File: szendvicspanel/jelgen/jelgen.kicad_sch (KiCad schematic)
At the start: 24 parts, among them J1 Conn_01x04_Pin, U1 TL072, U2 TL072

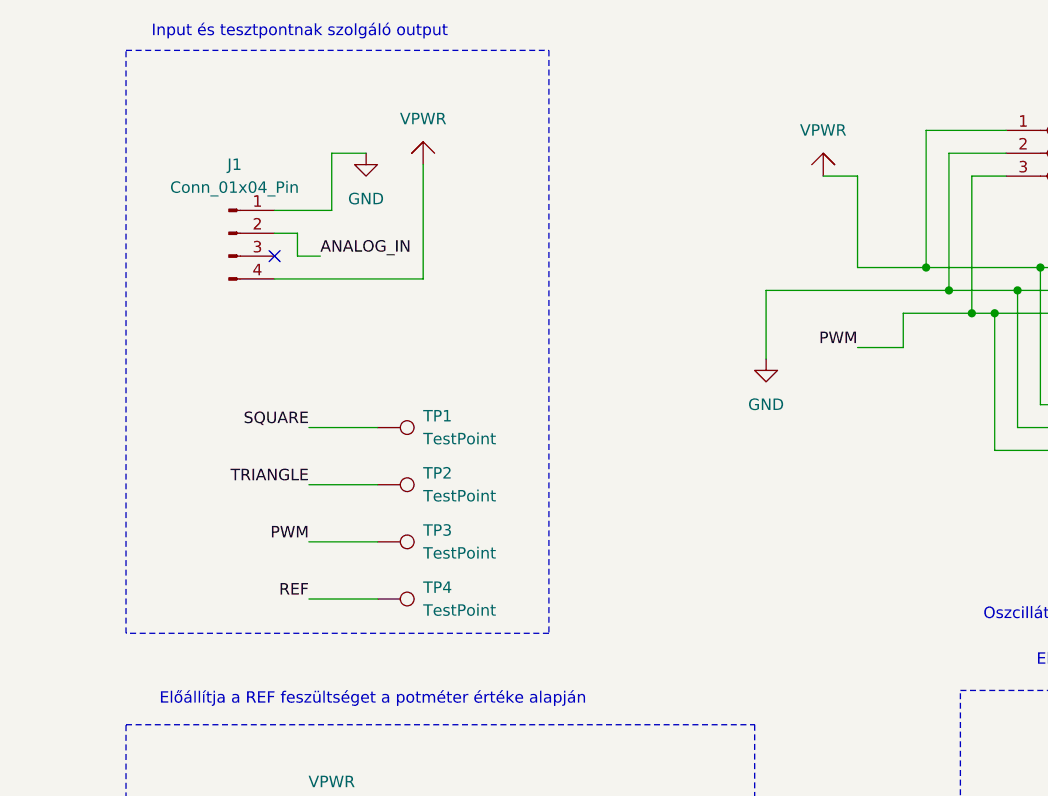
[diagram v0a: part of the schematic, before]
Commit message: Átalakítás a H-híd panel szélességére, hanging +5V input pin
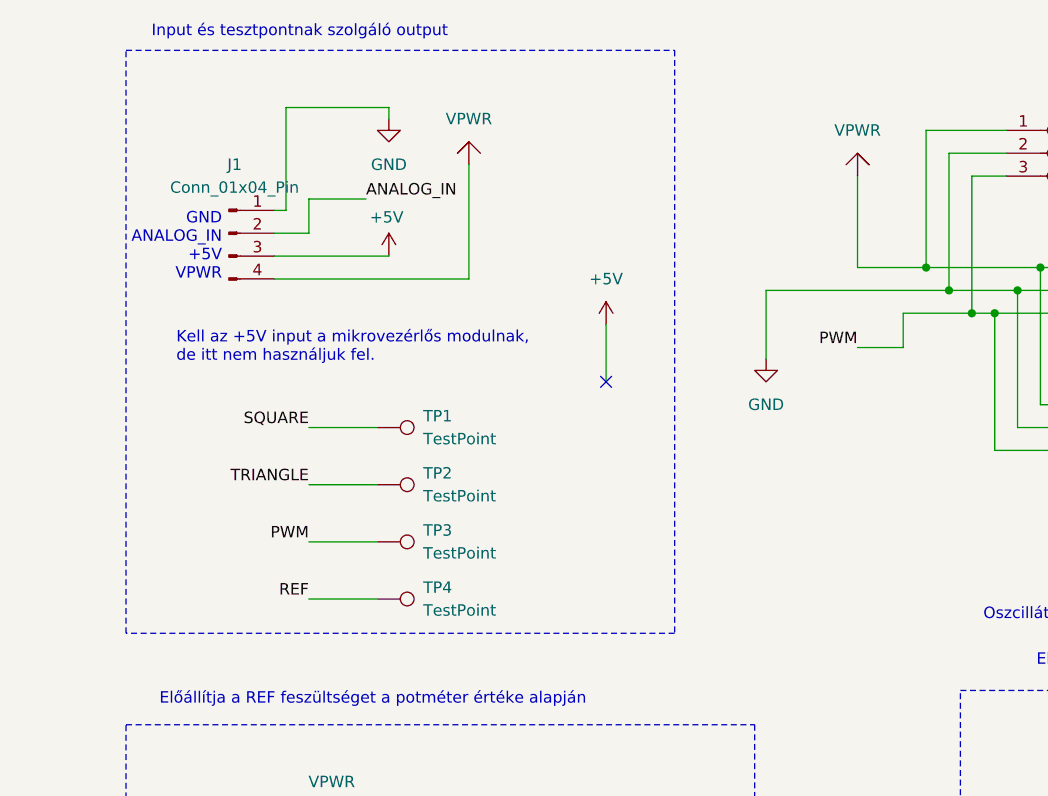
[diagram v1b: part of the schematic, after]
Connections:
- net +5V: now reaches J1.3 (Pin_3)
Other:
- note added: "GND ANALOG_IN +5V VPWR"
- note added: "Kell az +5V input a mikrovezérlős modulnak, de itt nem használjuk fel."
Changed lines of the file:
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@@
 	(rectangle
 		(start 30.48 22.86)
-		(end 77.47 87.63)
+		(end 91.44 87.63)
 		(stroke
 			(width 0.127)
@@
 		)
 	)
+	(text "GND\nANALOG_IN\n+5V\nVPWR"
+		(exclude_from_sim no)
+		(at 41.148 44.704 0)
+		(effects
+			(font
+				(size 1.27 1.27)
+			)
+			(justify right)
+		)
+	)
 	(text "Az oszcillátor háromszögjeléből és az analóg bemenetből előállítja a PWM jelet"
 		(exclude_from_sim no)
@@
 		)
 	)
+	(text "Kell az +5V input a mikrovezérlős modulnak,\nde itt nem használjuk fel."
+		(exclude_from_sim no)
+		(at 36.068 55.88 0)
+		(effects
+			(font
+				(size 1.27 1.27)
+			)
+			(justify left)
+		)
+	)
 	(text "8 db PWM output, 8 db H-hídhoz"
 		(exclude_from_sim no)
@@
 	)
 	(no_connect
-		(at 46.99 45.72)
+		(at 83.82 59.69)
 	)
 	(no_connect
@@
 	(wire
 		(pts
-			(xy 63.5 48.26) (xy 46.99 48.26)
+			(xy 68.58 48.26) (xy 46.99 48.26)
 		)
 		(stroke
@@
 	(wire
 		(pts
+			(xy 46.99 45.72) (xy 59.69 45.72)
+		)
+		(stroke
+			(width 0)
+			(type default)
+		)
+	)
+	(wire
+		(pts
 			(xy 153.67 46.99) (xy 166.37 46.99)
 		)
@@
 	(wire
 		(pts
-			(xy 53.34 34.29) (xy 57.15 34.29)
+			(xy 48.26 29.21) (xy 59.69 29.21)
+		)
+		(stroke
+			(width 0)
+			(type default)
+		)
+	)
+	(wire
+		(pts
+			(xy 59.69 29.21) (xy 59.69 30.48)
 		)
 		(stroke
@@
 	(wire
 		(pts
-			(xy 53.34 40.64) (xy 46.99 40.64)
+			(xy 48.26 40.64) (xy 46.99 40.64)
 		)
 		(stroke
@@
 	(wire
 		(pts
-			(xy 49.53 43.18) (xy 46.99 43.18)
+			(xy 50.8 39.37) (xy 57.15 39.37)
 		)
 		(stroke
@@
 	(wire
 		(pts
-			(xy 53.34 34.29) (xy 53.34 40.64)
+			(xy 48.26 29.21) (xy 48.26 40.64)
 		)
 		(stroke
@@
 	(wire
 		(pts
-			(xy 111.76 36.83) (xy 107.95 36.83)
-		)
-		(stroke
-			(width 0)
-			(type default)
-		)
-	)
-	(wire
-		(pts
 			(xy 102.87 175.26) (xy 93.98 175.26)
 		)
@@
 	(wire
 		(pts
+			(xy 50.8 43.18) (xy 46.99 43.18)
+		)
+		(stroke
+			(width 0)
+			(type default)
+		)
+	)
+	(wire
+		(pts
 			(xy 186.69 46.99) (xy 199.39 46.99)
 		)
@@
 	(wire
 		(pts
-			(xy 49.53 45.72) (xy 49.53 43.18)
-		)
-		(stroke
-			(width 0)
-			(type default)
-		)
-	)
-	(wire
-		(pts
 			(xy 83.82 123.19) (xy 91.44 123.19)
 		)
@@
 	(wire
 		(pts
-			(xy 52.07 45.72) (xy 49.53 45.72)
+			(xy 58.42 172.72) (xy 66.04 172.72)
 		)
 		(stroke
@@
 	(wire
 		(pts
-			(xy 58.42 172.72) (xy 66.04 172.72)
+			(xy 228.6 36.83) (xy 226.06 36.83)
 		)
 		(stroke
@@
 	(wire
 		(pts
-			(xy 228.6 36.83) (xy 226.06 36.83)
+			(xy 167.64 62.23) (xy 166.37 62.23)
 		)
 		(stroke
@@
 	(wire
 		(pts
-			(xy 167.64 62.23) (xy 166.37 62.23)
+			(xy 101.6 49.53) (xy 101.6 57.15)
 		)
 		(stroke
@@
 	(wire
 		(pts
-			(xy 101.6 49.53) (xy 101.6 57.15)
+			(xy 166.37 123.19) (xy 168.91 123.19)
 		)
 		(stroke
@@
 	(wire
 		(pts
-			(xy 166.37 123.19) (xy 168.91 123.19)
+			(xy 83.82 59.69) (xy 83.82 53.34)
 		)
 		(stroke
@@
 	(wire
 		(pts
-			(xy 63.5 35.56) (xy 63.5 48.26)
+			(xy 68.58 35.56) (xy 68.58 48.26)
 		)
 		(stroke
@@
 	(wire
 		(pts
+			(xy 50.8 39.37) (xy 50.8 43.18)
+		)
+		(stroke
+			(width 0)
+			(type default)
+		)
+	)
+	(wire
+		(pts
 			(xy 189.23 34.29) (xy 189.23 49.53)
 		)
@@
 	)
 	(label "ANALOG_IN"
-		(at 52.07 45.72 0)
+		(at 57.15 39.37 0)
 		(effects
 			(font
@@
 	(symbol
 		(lib_id "power:GND")
-		(at 57.15 34.29 0)
+		(at 59.69 30.48 0)
 		(unit 1)
 		(exclude_from_sim no)
@@
 		(fields_autoplaced yes)
 		(property "Reference" "#PWR01"
-			(at 57.15 40.64 0)
+			(at 59.69 36.83 0)
 			(effects
 				(font
@@
 		)
 		(property "Value" "GND"
-			(at 57.15 39.37 0)
+			(at 59.69 35.56 0)
 			(effects
 				(font
@@
 		)
 		(property "Footprint" ""
-			(at 57.15 34.29 0)
+			(at 59.69 30.48 0)
 			(effects
 				(font
@@
 		)
 		(property "Datasheet" ""
-			(at 57.15 34.29 0)
+			(at 59.69 30.48 0)
 			(effects
 				(font
@@
 		)
 		(property "Description" "Power symbol creates a global label with name \"GND\" , ground"
-			(at 57.15 34.29 0)
+			(at 59.69 30.48 0)
 			(effects
 				(font
@@
 	)
 	(symbol
+		(lib_id "power:+5V")
+		(at 83.82 53.34 0)
+		(unit 1)
+		(exclude_from_sim no)
+		(in_bom yes)
+		(on_board yes)
+		(dnp no)
+		(fields_autoplaced yes)
+		(property "Reference" "#PWR08"
+			(at 83.82 57.15 0)
+			(effects
+				(font
+					(size 1.27 1.27)
+				)
+				(hide yes)
+			)
+		)
+		(property "Value" "+5V"
+			(at 83.82 48.26 0)
+			(effects
+				(font
+					(size 1.27 1.27)
+				)
+			)
+		)
+		(property "Footprint" ""
+			(at 83.82 53.34 0)
+			(effects
+				(font
+					(size 1.27 1.27)
+				)
+				(hide yes)
+			)
+		)
+		(property "Datasheet" ""
+			(at 83.82 53.34 0)
+			(effects
+				(font
+					(size 1.27 1.27)
+				)
+				(hide yes)
+			)
+		)
+		(property "Description" "Power symbol creates a global label with name \"+5V\""
+			(at 83.82 53.34 0)
+			(effects
+				(font
+					(size 1.27 1.27)
+				)
+				(hide yes)
+			)
+		)
+		(pin "1"
+		)
+		(instances
+			(project ""
+				(path "/38c57eff-28aa-412a-a0ac-28961721bf2b"
+					(reference "#PWR08")
+					(unit 1)
+				)
+			)
+		)
+	)
+	(symbol
 		(lib_id "Device:C")
 		(at 176.53 137.16 90)
@@
 	)
 	(symbol
+		(lib_id "power:+5V")
+		(at 59.69 45.72 0)
+		(unit 1)
+		(exclude_from_sim no)
+		(in_bom yes)
+		(on_board yes)
+		(dnp no)
+		(property "Reference" "#PWR04"
+			(at 59.69 49.53 0)
+			(effects
+				(font
+					(size 1.27 1.27)
+				)
+				(hide yes)
+			)
+		)
+		(property "Value" "+5V"
+			(at 59.436 41.402 0)
+			(effects
+				(font
+					(size 1.27 1.27)
+				)
+			)
+		)
+		(property "Footprint" ""
+			(at 59.69 45.72 0)
+			(effects
+				(font
+					(size 1.27 1.27)
+				)
+				(hide yes)
+			)
+		)
+		(property "Datasheet" ""
+			(at 59.69 45.72 0)
+			(effects
+				(font
+					(size 1.27 1.27)
+				)
+				(hide yes)
+			)
+		)
+		(property "Description" "Power symbol creates a global label with name \"+5V\""
+			(at 59.69 45.72 0)
+			(effects
+				(font
+					(size 1.27 1.27)
+				)
+				(hide yes)
+			)
+		)
+		(pin "1"
+		)
+		(instances
+			(project ""
+				(path "/38c57eff-28aa-412a-a0ac-28961721bf2b"
+					(reference "#PWR04")
+					(unit 1)
+				)
+			)
+		)
+	)
+	(symbol
 		(lib_id "Connector:Conn_01x03_Socket")
 		(at 139.7 64.77 0)
@@
 	(symbol
 		(lib_id "custom_symbols:VPWR")
-		(at 63.5 35.56 0)
+		(at 68.58 35.56 0)
 		(unit 1)
 		(exclude_from_sim no)
@@
 		(fields_autoplaced yes)
 		(property "Reference" "#VPWR01"
-			(at 63.5 35.56 0)
+			(at 68.58 35.56 0)
 			(effects
 				(font
@@
 		)
 		(property "Value" "VPWR"
-			(at 63.5 30.48 0)
+			(at 68.58 30.48 0)
 			(effects
 				(font
@@
 		)
 		(property "Footprint" ""
-			(at 63.5 35.56 0)
+			(at 68.58 35.56 0)
 			(effects
 				(font
@@
 		)
 		(property "Datasheet" ""
-			(at 63.5 35.56 0)
+			(at 68.58 35.56 0)
 			(effects
 				(font
@@
 		)
 		(property "Description" "Saját VPWR szimbólum - 16-18V"
-			(at 63.5 35.56 0)
+			(at 68.58 35.56 0)
 			(effects
 				(font
@@
 	(symbol
 		(lib_id "custom_symbols:VPWR")
-		(at 107.95 36.83 0)
+		(at 111.76 36.83 0)
 		(mirror y)
 		(unit 1)
@@
 		(dnp no)
 		(property "Reference" "#VPWR05"
-			(at 107.95 36.83 0)
+			(at 111.76 36.83 0)
 			(effects
 				(font
@@
 		)
 		(property "Value" "VPWR"
-			(at 107.95 31.75 0)
+			(at 111.76 31.75 0)
 			(effects
 				(font
@@
 		)
 		(property "Footprint" ""
-			(at 107.95 36.83 0)
+			(at 111.76 36.83 0)
 			(effects
 				(font
@@
 		)
 		(property "Datasheet" ""
-			(at 107.95 36.83 0)
+			(at 111.76 36.83 0)
 			(effects
 				(font
@@
 		)
 		(property "Description" "Saját VPWR szimbólum - 16-18V"
-			(at 107.95 36.83 0)
+			(at 111.76 36.83 0)
 			(effects
 				(font

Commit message: Analóg jelgen fix WIP
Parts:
- OJ1, OJ2, OJ3, OJ4, OJ5, OJ6, OJ7, OJ8: footprint Connector_PinSocket_2.54mm:PinSocket_1x03_P2.54mm_Vertical -> sajat:sajat_pin3
- U1, U2: footprint Package_DIP:DIP-8_W7.62mm -> Package_DIP:DIP-8_W7.62mm_LongPads
